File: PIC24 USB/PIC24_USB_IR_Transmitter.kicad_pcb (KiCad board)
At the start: 2 copper layers, 86.4 x 48.3 mm, 64 parts, among them CON1 USB-MINI-B, P1 CONN_6, P2 CONN_4, P3 CONN_4, P4 CONN_8, P5 CONN_4, P6 CONN_1, P7 CONN_8, P8 CONN_8X2, Q1 2N7002, Q2 2N7002, Q3 2N7002, Q4 2N7002, Q5 2N7002, Q6 2N7002, U1 PIC24FJXXXGB106, U2 LM1117_SOT223_3V3, U3 50mm_5x7_Dot_Matrix_Led_Displ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, U4 MCP48X2, U5 MCP9700, U6 24C16, U7 TCN75, X1 CRYSTAL_12MHZ, X2 32khz

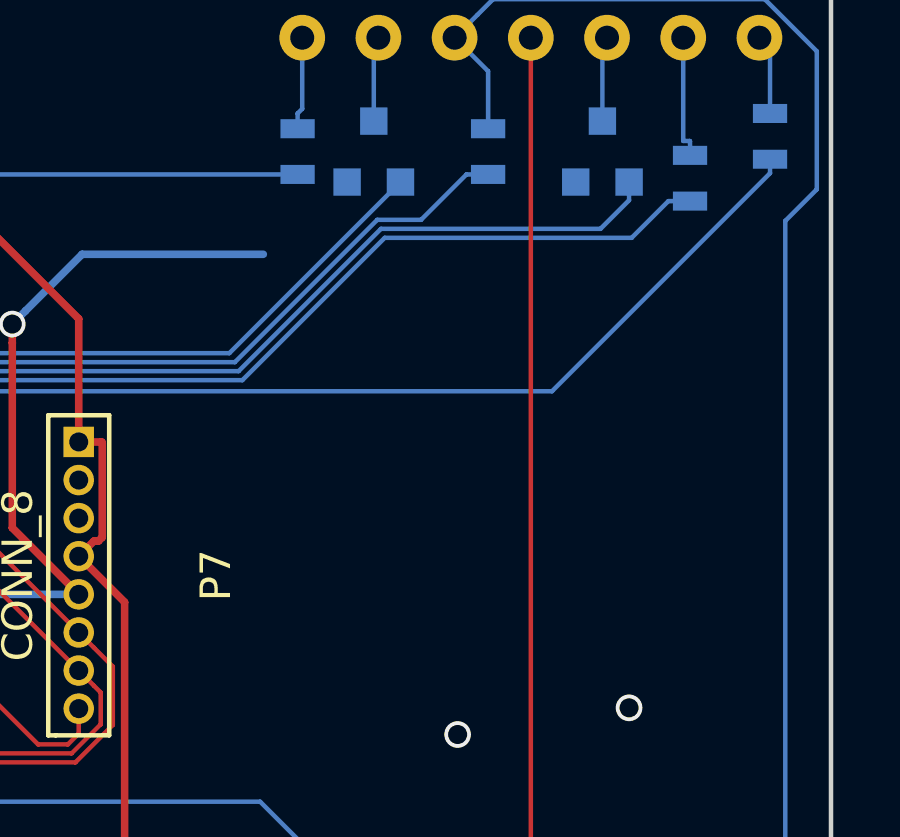
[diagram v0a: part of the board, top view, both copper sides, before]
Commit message: Update PIC16F USB Board and PIC 24F/32 USB board
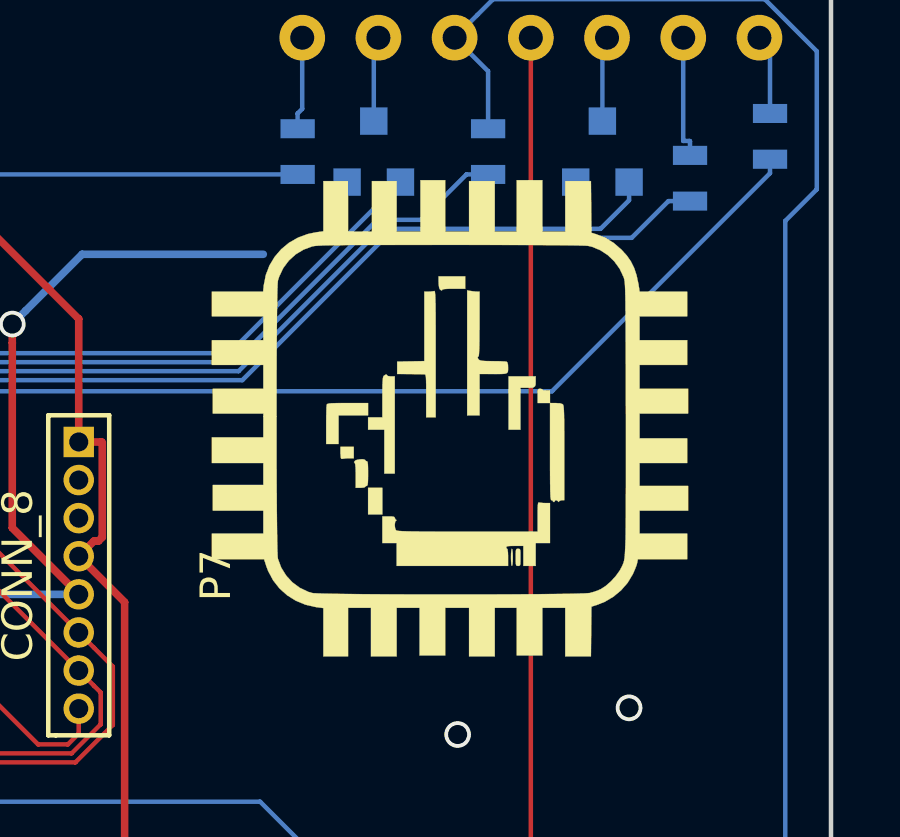
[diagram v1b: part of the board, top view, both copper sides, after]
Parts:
- added G***: LOGO, PIC24 USB:fingerchip_Logo, F.Cu at (97.8, 31.8)
- added G***: LOGO, PIC24 USB:fingerchip_Logo, B.Cu at (38.1, 45.7)
